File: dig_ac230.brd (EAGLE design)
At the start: 100 x 85 mm, 142 parts, among them IC201 ATMEGA32A-AU, IC202 DS1337S, IC203 MAX487CSA, IC204 74HC166D, IC301 LTV-356T, IC302 LTV-356T, IC303 LTV-356T, IC304 LTV-356T, IC305 LTV-356T, IC306 LTV-356T, IC307 LTV-356T, IC308 LTV-356T, IC401 74HC595D, K401 S202S02, K402 S202S02, K403 S202S02, K404 S202S02, K405 S202S02, K406 S202S02, K407 S202S02, K408 S202S02, Q201 32,768kHz, Q301 BCR191, Q302 BCR191, Q303 BCR191, Q304 BCR191, Q305 BCR191, Q306 BCR191, Q307 BCR191, Q308 BCR191, X101 RIA-73-02, X201 ISP, X202 RIA-73-02, X301 RIA-73-02, X302 RIA-73-02, X303 RIA-73-02, X304 RIA-73-02, X305 RIA-73-02, X401 RIA-73-02, X402 RIA-73-02, X403 RIA-73-02, X404 RIA-73-02, X405 RIA-73-02

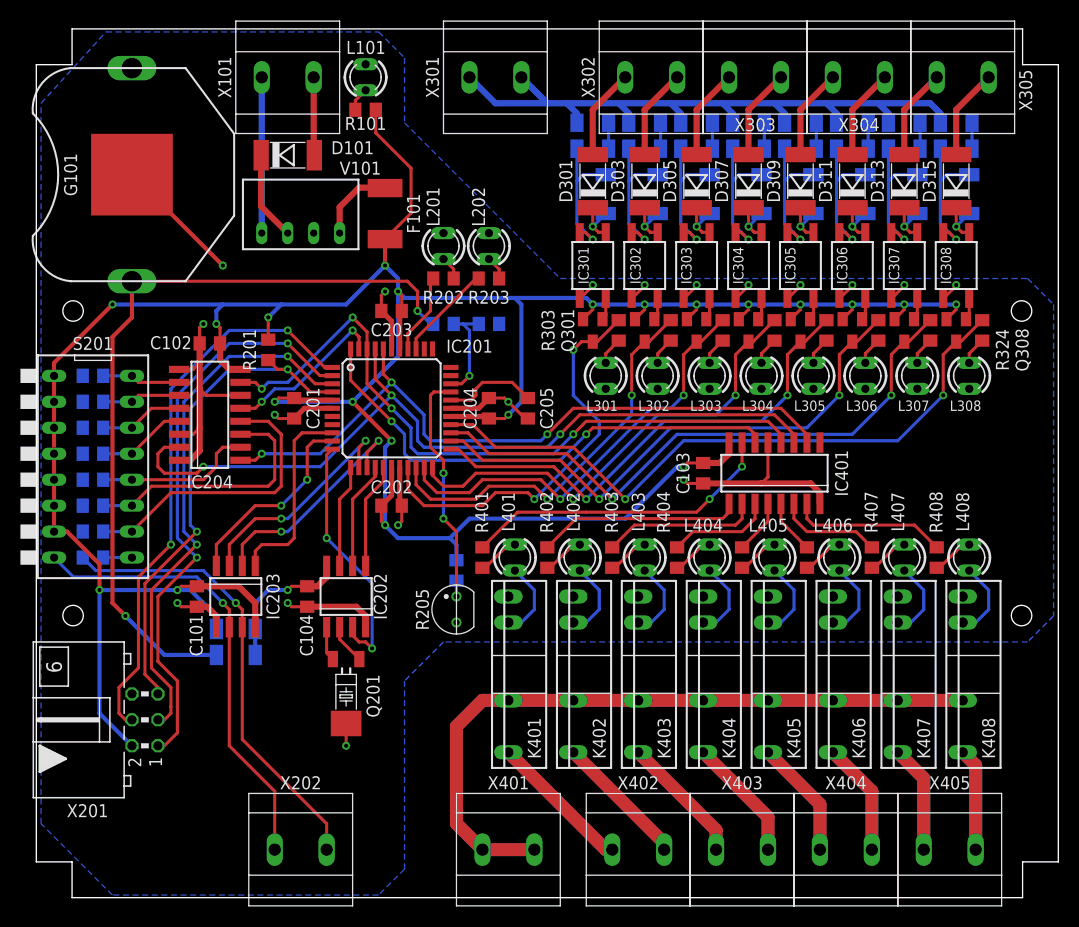
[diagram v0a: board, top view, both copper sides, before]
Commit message: Eingänge auf ltv-354t umgestellt
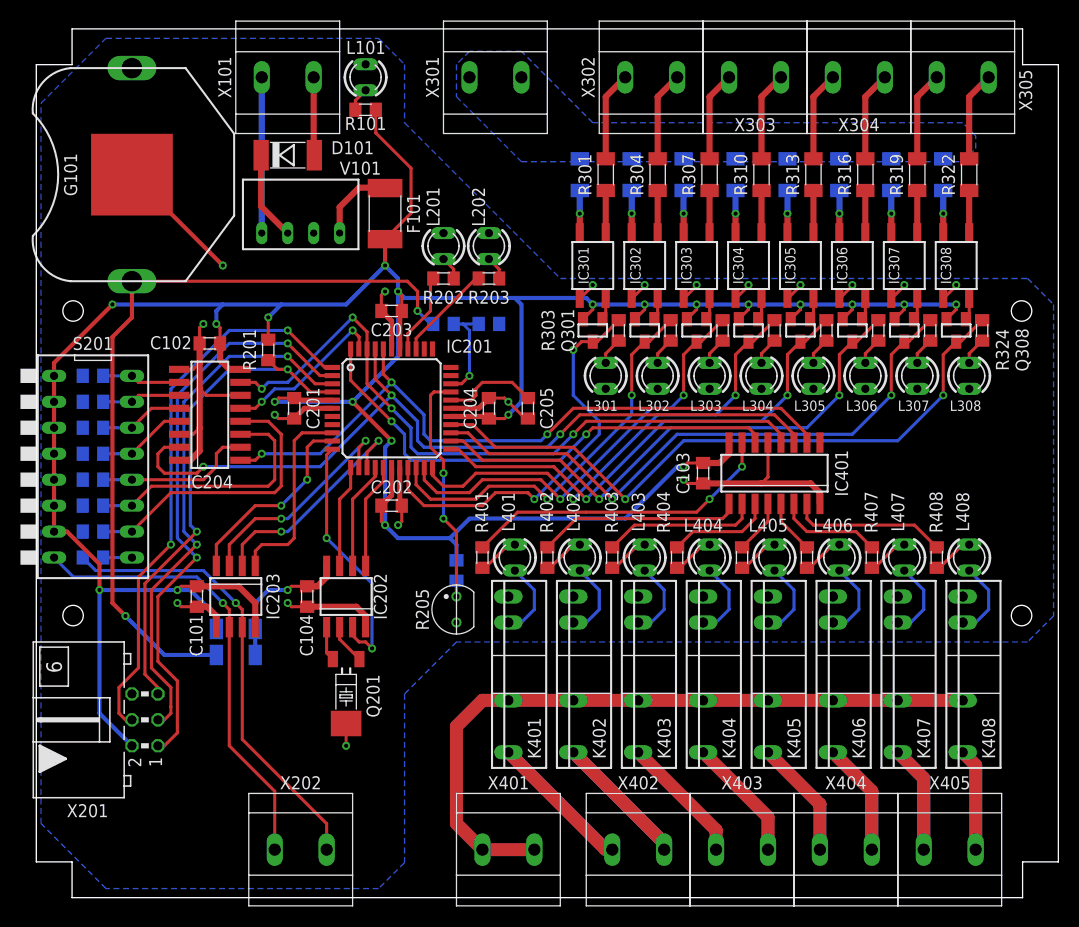
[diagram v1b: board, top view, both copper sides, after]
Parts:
- removed D301, D303, D305, D307, D309, D311, D313, D315: DL4007, diode:MELF
- removed D302, D304, D306, D308, D310, D312, D314, D316: 1N4148, diode:MINIMELF
- IC301, IC302, IC303, IC304, IC305, IC306, IC307, IC308: value LTV-356T -> LTV-354T
- moved R317 5.24 mm to (80.6, 71.1), turned to 270 degrees
- moved R320 5.24 mm to (85.7, 71.1), turned to 270 degrees
- moved R302 5.24 mm to (55.2, 71.1), turned to 270 degrees
- moved R305 5.24 mm to (60.3, 71.1), turned to 270 degrees
- moved R308 5.24 mm to (65.4, 71.1), turned to 270 degrees
- moved R311 5.24 mm to (70.5, 71.1), turned to 270 degrees
- moved R314 5.24 mm to (75.6, 71.1), turned to 270 degrees
- moved R323 5.24 mm to (90.8, 71.1), turned to 270 degrees
- moved R310 2.84 mm to (73.0, 71.1), flipped to the top, turned to 90 degrees
- moved R313 2.84 mm to (78.1, 71.1), flipped to the top, turned to 90 degrees
- moved R304 2.84 mm to (62.9, 71.1), flipped to the top, turned to 90 degrees
- moved R301 2.84 mm to (57.8, 71.1), flipped to the top, turned to 90 degrees
- moved R307 2.84 mm to (67.9, 71.1), flipped to the top, turned to 90 degrees
- moved R316 2.84 mm to (83.2, 71.1), flipped to the top, turned to 90 degrees
- moved R319 2.84 mm to (88.3, 71.1), flipped to the top, turned to 90 degrees
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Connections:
- removed net N$100: D313.A, X305.2
- removed net N$101: D315.A, X305.1
- removed net N$86: D301.A, X302.2
- removed net N$87: D303.A, X302.1
- removed net N$88: D305.A, X303.2
- removed net N$91: D307.A, X303.1
- removed net N$94: D309.A, X304.2
- removed net N$97: D311.A, X304.1
- net N$1: now also R301.2, X302.2; no longer D301.K, D302.K, IC301.1
- net N$10: now also R310.2, X303.1; no longer D310.A, IC305.2, R313.2
- net N$11: now also IC304.1, R310.1; no longer D311.K, D312.K, IC306.1
- net N$12: now also IC304.2, R311.2; no longer D312.A, IC306.2, R316.2
- net N$13: now also R313.2, X304.2; no longer D313.K, D314.K, IC307.1
- net N$14: now also IC305.1, R313.1; no longer D314.A, IC307.2, R319.2
- net N$15: now also IC305.2, R314.2; no longer D315.K, D316.K, IC308.1
- net N$16: now also R316.2, X304.1; no longer D316.A, IC308.2, R322.2
- net N$2: now also IC301.1, R301.1; no longer D302.A, IC301.2, R301.2
- net N$3: now also IC301.2, R302.2; no longer D303.K, D304.K, IC302.1
- net N$35: now also IC306.1, R316.1; no longer R301.1, R302.2
- net N$37: now also IC306.2, R317.2; no longer R304.1, R305.2
- net N$39: now also IC307.1, R319.1; no longer R307.1, R308.2
- net N$4: now also X302.1; no longer D304.A, IC302.2
- net N$5: now also IC302.1, R304.1; no longer D305.K, D306.K, IC303.1
- net N$50: now also IC307.2, R320.2; no longer R310.1, R311.2
- net N$57: now also R319.2, X305.2; no longer R313.1, R314.2
- net N$6: now also IC302.2, R305.2; no longer D306.A, IC303.2, R307.2
- net N$67: now also R322.2, X305.1; no longer R316.1, R317.2
- net N$7: now also R307.2, X303.2; no longer D307.K, D308.K, IC304.1
- net N$71: now also IC308.1, R322.1; no longer R319.1, R320.2
- net N$79: now also IC308.2; no longer R322.1
- net N$8: now also IC303.1, R307.1; no longer D308.A, IC304.2, R310.2
- net N$9: now also IC303.2, R308.2; no longer D309.K, D310.K, IC305.1
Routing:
- net GNDIO: track 71.8 -> 0.00 mm
- net N$14: track 14.2 -> 4.09 mm, vias 1 -> 0
- net N$12: track 14.2 -> 4.09 mm
- net N$8: track 14.2 -> 4.09 mm, vias 1 -> 0
- net N$2: track 14.2 -> 4.09 mm, vias 1 -> 0
- net N$6: track 14.2 -> 4.09 mm
- net N$94: track 8.88 -> 0.00 mm
- net N$91: track 8.88 -> 0.00 mm
- net N$97: track 8.88 -> 0.00 mm
- net N$88: track 8.88 -> 0.00 mm
- net N$87: track 8.88 -> 0.00 mm
- net N$86: track 8.88 -> 0.00 mm
- net N$101: track 8.88 -> 0.00 mm
- net N$100: track 8.88 -> 0.00 mm
- net N$67: track 2.54 -> 8.76 mm
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- added copper zone on layer 16, net GNDIO

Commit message: Bezeichnungen angepasst; Position auf Board angepasst
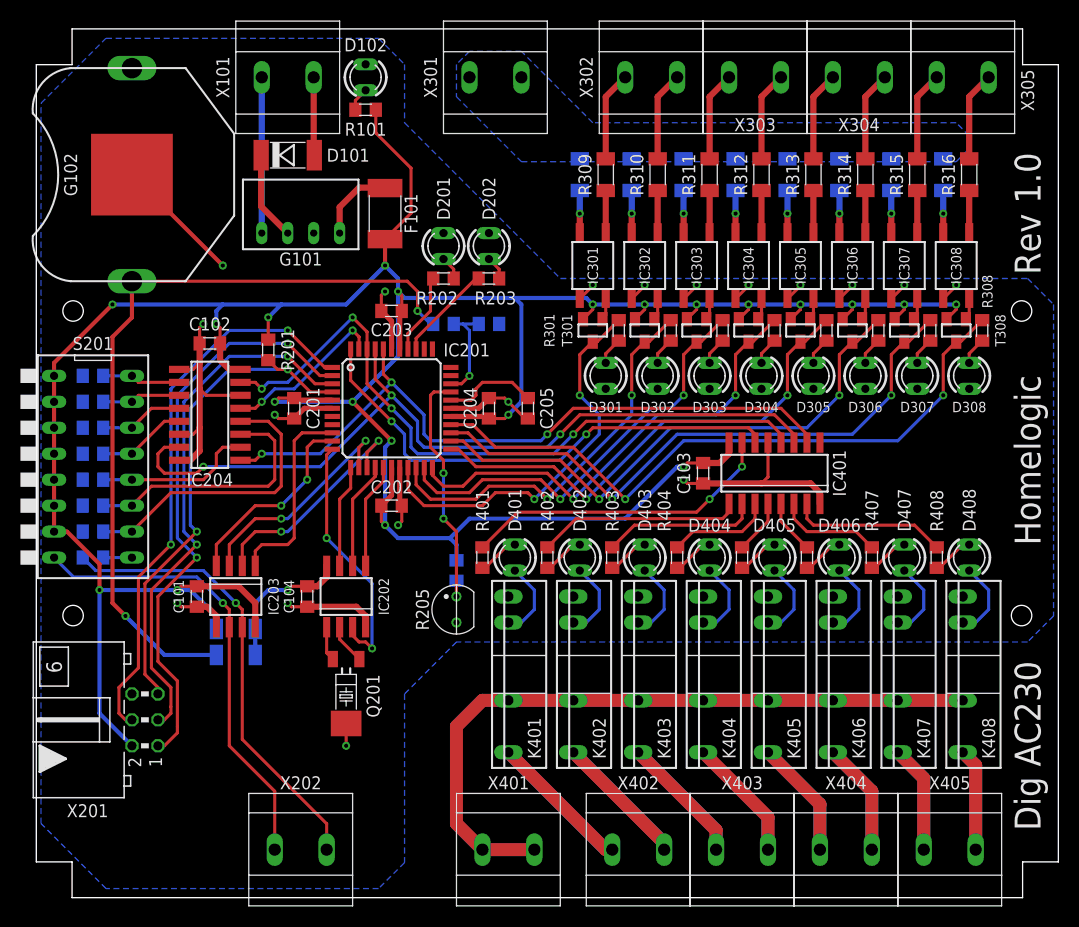
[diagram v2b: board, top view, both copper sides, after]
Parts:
- removed L101: GN, led:LED3MM
- removed V101: TME2405S, schaltregler:TME-24V
- added D104: 1N4148, diode:MINIMELF
- added G102: KZH20P, batterie:KZH20P
- D102: value 1N4148 -> GN; device diode:MINIMELF -> led:LED3MM
- G101: value KZH20P -> TME2405S; device batterie:KZH20P -> schaltregler:TME-24V
- R301, R302, R304, R305, R307, R308: value 120kΩ -> 390Ω; device passiv:CHIP_1206 -> passiv:CHIP_0805
- R309, R312, R315, R318, R321, R324: value 390Ω -> 120kΩ; device passiv:CHIP_0805 -> passiv:CHIP_1206
- moved D102 55.4 mm to (34.3, 80.6), flipped to the top, turned to 90 degrees
- moved R308 32.9 mm to (94.6, 55.9), flipped to the top, turned to 90 degrees
- moved R318 28.5 mm to (60.3, 71.1), flipped to the bottom, turned to 270 degrees
- moved R307 26.4 mm to (89.5, 55.9)
- moved R317 25.4 mm to (55.2, 71.1)
- moved R305 24.4 mm to (79.4, 55.9), flipped to the top, turned to 90 degrees
- moved R319 22.9 mm to (65.4, 71.1), flipped to the bottom, turned to 270 degrees
- moved R321 20.7 mm to (75.6, 71.1), flipped to the bottom, turned to 270 degrees
- moved R306 20.3 mm to (84.5, 55.9)
- moved R304 19.1 mm to (74.3, 55.9)
- moved R309 19.1 mm to (57.8, 71.1)
- moved R302 17.6 mm to (64.1, 55.9), flipped to the top, turned to 90 degrees
- moved R315 17.6 mm to (88.3, 71.1)
- moved G101 17.5 mm to (27.9, 65.4), turned to 0 degrees
- moved R324 15.7 mm to (90.8, 71.1), flipped to the bottom, turned to 270 degrees
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- renumbered L201 to D201, L202 to D202, L301 to D301, L302 to D302, L303 to D303, L304 to D304, L305 to D305, L306 to D306, L307 to D307, L308 to D308, L401 to D401, L402 to D402, L403 to D403, L404 to D404, L405 to D405, L406 to D406, L407 to D407, L408 to D408, Q301 to T301, Q302 to T302, Q303 to T303, Q304 to T304, Q305 to T305, Q306 to T306, Q307 to T307, Q308 to T308
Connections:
- net +5V: now also D103.A; no longer D102.A
- net GND: now also D102.K, G101.3, G102.N; no longer G101.N, L101.K, V101.3
- net GNDIO: now also R318.1, R319.1, R321.1, R322.1, R324.1; no longer R302.1, R305.1, R308.1, R311.1, R314.1
- net IN0: now also R301.2; no longer R303.2
- net IN1: now also R302.2; no longer R306.2
- net IN2: now also R303.2; no longer R309.2
- net IN3: now also R304.2; no longer R312.2
- net IN4: now also R305.2; no longer R315.2
- net IN5: now also R306.2; no longer R318.2
- net IN6: now also R307.2; no longer R321.2
- net IN7: now also R308.2; no longer R324.2
- net N$1: now also R309.2; no longer R301.2
- net N$10: now also R312.2; no longer R310.2
- net N$11: now also R312.1; no longer R310.1
- net N$12: now also R320.2; no longer R311.2
- net N$15: now also R321.2; no longer R314.2
- net N$16: now also R314.2; no longer R316.2
- net N$19: now also G101.1; no longer V101.1
- net N$2: now also R309.1; no longer R301.1
- net N$21: now also D104.A, G102.P1, G102.P2; no longer D103.A, G101.P1, G101.P2
- net N$23: now also G101.2; no longer V101.2
- net N$3: now also R317.2; no longer R302.2
- net N$34: now also R304.1; no longer R312.1
- net N$35: now also R314.1; no longer R316.1
- net N$36: now also R303.1; no longer R309.1
- net N$37: now also R322.2; no longer R317.2
- net N$38: now also R302.1; no longer R306.1
- net N$39: now also R315.1; no longer R319.1
- net N$4: now also R310.2; no longer R304.2
- net N$40: now also R301.1; no longer R303.1
- net N$41: now also G101.4; no longer V101.4
- net N$44: now also D102.A; no longer L101.A
- net N$5: now also R310.1; no longer R304.1
- net N$50: now also R323.2; no longer R320.2
- net N$55: now also R305.1; no longer R315.1
- net N$57: now also R315.2; no longer R319.2
- net N$6: now also R318.2; no longer R305.2
- net N$64: now also D104.K; no longer D102.K
- net N$65: now also R306.1; no longer R318.1
- net N$67: now also R316.2; no longer R322.2
- net N$69: now also R307.1; no longer R321.1
- net N$7: now also R311.2; no longer R307.2
- net N$71: now also R316.1; no longer R322.1
- net N$77: now also R308.1; no longer R324.1
- net N$79: now also R324.2; no longer R323.2
- net N$8: now also R311.1; no longer R307.1
- net N$9: now also R319.2; no longer R308.2
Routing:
- net IN0: track 39.9 -> 38.7 mm
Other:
- board text added: "Dig AC230"
- board text added: "Homelogic"
- board text added: "Rev 1.0"

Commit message: Wert von D101 geändert
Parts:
- D101: value TMBAT49 -> LL5819
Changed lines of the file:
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@@
 <attribute name="VALUE" x="22.86" y="67.945" size="1.27" layer="27"/>
 </element>
-<element name="D101" library="diode" package="MELF" value="TMBAT49" x="26.67" y="73.025" smashed="yes">
+<element name="D101" library="diode" package="MELF" value="LL5819" x="26.67" y="73.025" smashed="yes">
 <attribute name="NAME" x="30.48" y="73.025" size="1.27" layer="25" align="center-left"/>
 <attribute name="VALUE" x="26.67" y="71.025" size="1.27" layer="27" align="top-center"/>

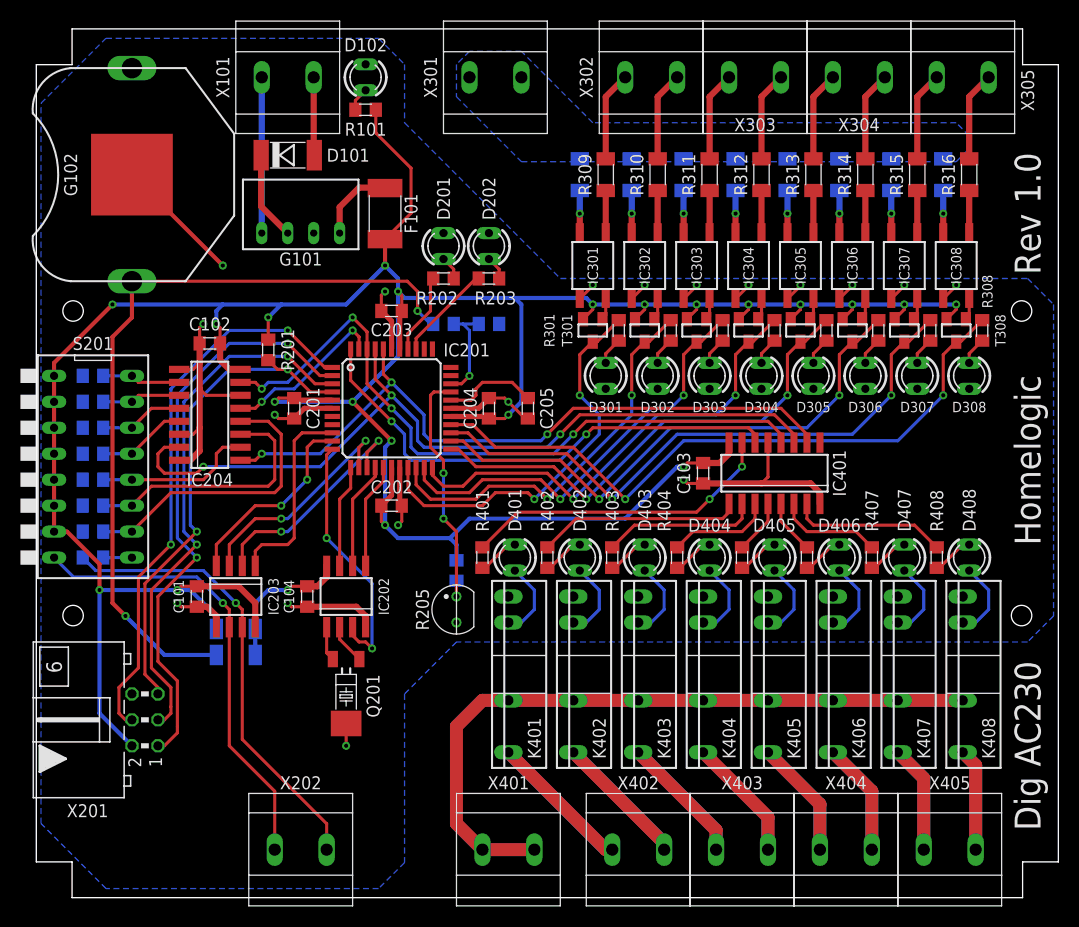
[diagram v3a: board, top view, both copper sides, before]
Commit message: Anschlüsse versetzt
  Anschlüsse sind jetzt nicht mehr korrekt unter den Löchern dafür
  müsste die Platine aber ins Gehäuse passen
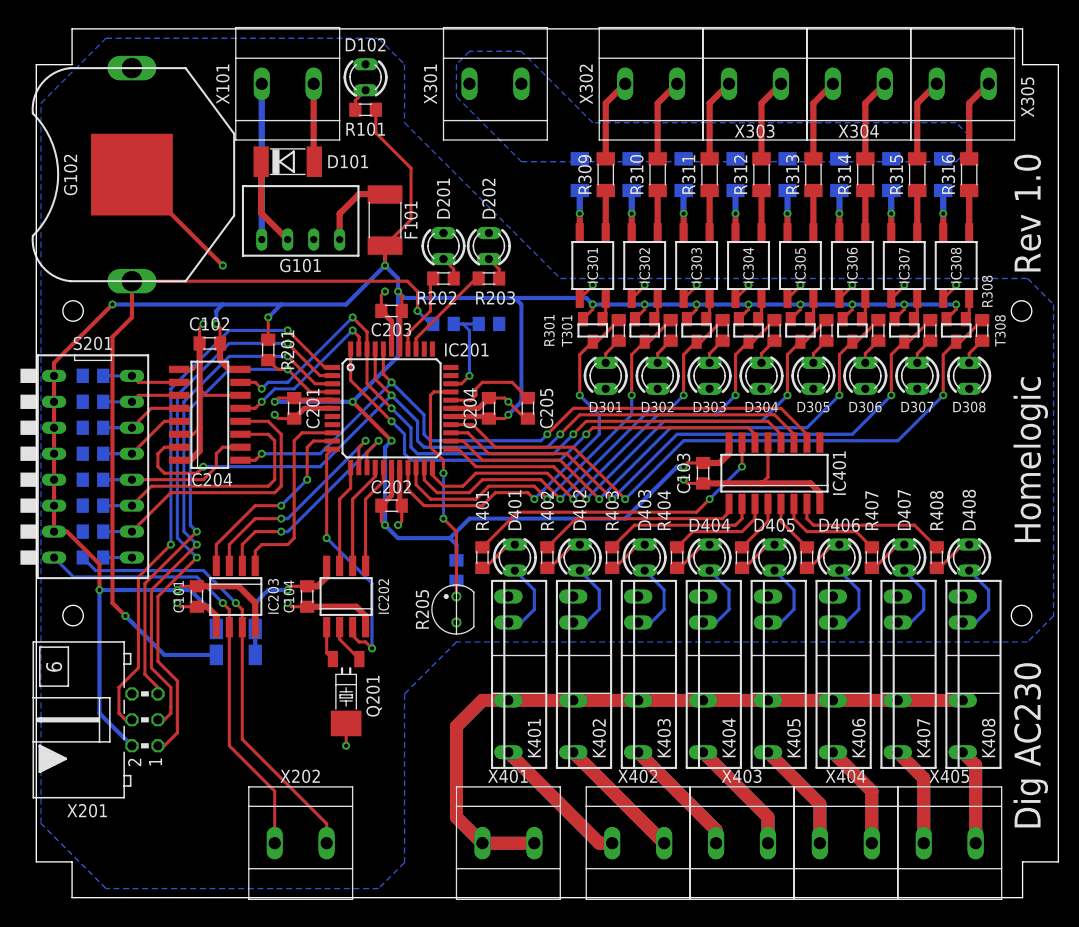
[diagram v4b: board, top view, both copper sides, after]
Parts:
- moved D101 0.64 mm to (26.7, 72.4)
- moved F101 0.64 mm to (36.2, 66.7)
- moved G101 0.64 mm to (27.9, 64.8)
- moved X202 0.63 mm to (27.9, 5.71)
- moved X401 0.63 mm to (48.3, 5.71)
- moved X402 0.63 mm to (61.0, 5.71)
- moved X403 0.63 mm to (71.1, 5.71)
- moved X404 0.63 mm to (81.3, 5.71)
- moved X405 0.63 mm to (91.4, 5.71)
- moved X101 0.63 mm to (26.7, 80.0)
- moved X301 0.63 mm to (47.0, 80.0)
- moved X302 0.63 mm to (62.2, 80.0)
- moved X303 0.63 mm to (72.4, 80.0)
- moved X304 0.63 mm to (82.5, 80.0)
- moved X305 0.63 mm to (92.7, 80.0)
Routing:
- net L: track 137.6 -> 136.3 mm
- net N$78: track 23.3 -> 22.0 mm
- net N$76: track 24.3 -> 23.0 mm
- net N$74: track 25.4 -> 24.1 mm
- net N$89: track 20.1 -> 18.8 mm
- net N$84: track 21.2 -> 19.9 mm
- net N$82: track 22.2 -> 20.9 mm
- net N$72: track 26.4 -> 25.1 mm
- net N$22: track 44.6 -> 44.0 mm
- net N$7: track 8.76 -> 8.13 mm
- net N$67: track 8.76 -> 8.13 mm
- net N$57: track 8.76 -> 8.13 mm
- net N$4: track 8.76 -> 8.13 mm
- net N$20: track 44.6 -> 44.0 mm
- net N$16: track 8.76 -> 8.13 mm
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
